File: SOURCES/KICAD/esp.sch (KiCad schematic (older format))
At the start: 14 parts, among them IC501 ESP32-WROOM-32U, Q501 Q_SS8050-G, Q502 Q_SS8050-G, SW501 SW_Push, X501 Conn_01x04, X502 Conn_01x05, X503 Conn_01x03, X504 HDR_01x06

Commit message: Updated BOM
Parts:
- C501, C503: Manufacturer (none) -> KEMET; pn (none) -> C0805C104K5RACTU
- C502: Manufacturer (none) -> Murata Electronics North America; pn (none) -> GRM21BR61E106MA73L
- IC501: Manufacturer (none) -> Espressif Systems; pn (none) -> ESP32-WROOM-32U
- Q501, Q502: Manufacturer (none) -> Comchip Technology; pn (none) -> SS8050-G
- R501, R502, R503: Manufacturer (none) -> Yageo; pn (none) -> RC0805FR-0710KL
- SW501: Manufacturer (none) -> Omron Electronics Inc-EMC Div; pn (none) -> B3U-1000P
- X501: Manufacturer (none) -> Molex, LLC; pn (none) -> 0022232041
- X502: Manufacturer (none) -> Molex, LLC; pn (none) -> 0530470510
- X503: Manufacturer (none) -> Molex, LLC; pn (none) -> 0530470310
- X504: Manufacturer (none) -> Sullins Connector Solutions; pn (none) -> PRPC006SAAN-RC
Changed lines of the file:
@@
 F 5 "Module" H 0   0   50  0001 C CNN "Value2"
 F 6 "1904-1026-1-ND" H 0   0   50  0001 C CNN "digikey"
+F 7 "Espressif Systems" H 0   0   50  0001 C CNN "Manufacturer"
+F 8 "ESP32-WROOM-32U" H 0   0   50  0001 C CNN "pn"
 	1    5600 3050
 	1    0    0    -1
@@
 F 5 "1% 0.125W Thick" H 3550 2525 39  0001 C CNN "Value2"
 F 6 "311-10.0KCRCT-ND" H 3550 2350 39  0001 C CNN "digikey"
+F 7 "Yageo" H 0   0   50  0001 C CNN "Manufacturer"
+F 8 "RC0805FR-0710KL" H 0   0   50  0001 C CNN "pn"
 	1    3550 2650
 	1    0    0    -1
@@
 F 5 "5% 50V X7R" H 3950 2600 39  0001 C CNN "Value2"
 F 6 "399-1170-1-ND" H 3950 2550 39  0001 C CNN "digikey"
+F 7 "KEMET" H 0   0   50  0001 C CNN "Manufacturer"
+F 8 "C0805C104K5RACTU" H 0   0   50  0001 C CNN "pn"
 	1    3950 2850
 	0    -1   -1   0
@@
 F 5 "5% 50V X7R" H 4350 2600 39  0001 C CNN "Value2"
 F 6 "399-1170-1-ND" H 4350 2550 39  0001 C CNN "digikey"
+F 7 "KEMET" H 0   0   50  0001 C CNN "Manufacturer"
+F 8 "C0805C104K5RACTU" H 0   0   50  0001 C CNN "pn"
 	1    4350 2850
 	0    -1   -1   0
@@
 F 5 "20% 25V X5R" H 4150 2600 39  0001 C CNN "Value2"
 F 6 "490-10748-1-ND" H 4150 2550 39  0001 C CNN "digikey"
+F 7 "Murata Electronics North America" H 0   0   50  0001 C CNN "Manufacturer"
+F 8 "GRM21BR61E106MA73L" H 0   0   50  0001 C CNN "pn"
 	1    4150 2850
 	0    -1   -1   0
@@
 F 5 "-" H 0   0   50  0001 C CNN "Value2"
 F 6 "???" H 0   0   50  0001 C CNN "digikey"
+F 7 "Molex, LLC" H 0   0   50  0001 C CNN "Manufacturer"
+F 8 "0022232041" H 0   0   50  0001 C CNN "pn"
 	1    8100 2100
 	1    0    0    1
@@
 F 5 "-" H 0   0   50  0001 C CNN "Value2"
 F 6 "???" H 0   0   50  0001 C CNN "digikey"
+F 7 "Molex, LLC" H 0   0   50  0001 C CNN "Manufacturer"
+F 8 "0530470510" H 0   0   50  0001 C CNN "pn"
 	1    8100 2950
 	1    0    0    1
@@
 F 5 "-" H 0   0   50  0001 C CNN "Value2"
 F 6 "???" H 0   0   50  0001 C CNN "digikey"
+F 7 "Molex, LLC" H 0   0   50  0001 C CNN "Manufacturer"
+F 8 "0530470310" H 0   0   50  0001 C CNN "pn"
 	1    8100 4000
 	1    0    0    1
@@
 F 5 "-" H 0   0   50  0001 C CNN "Value2"
 F 6 "???" H 0   0   50  0001 C CNN "digikey"
+F 7 "Sullins Connector Solutions" H 0   0   50  0001 C CNN "Manufacturer"
+F 8 "PRPC006SAAN-RC" H 0   0   50  0001 C CNN "pn"
 	1    7750 5200
 	1    0    0    -1
@@
 F 5 "1% 0.125W Thick" H 5250 5075 39  0001 C CNN "Value2"
 F 6 "311-10.0KCRCT-ND" H 5250 4900 39  0001 C CNN "digikey"
+F 7 "Yageo" H 0   0   50  0001 C CNN "Manufacturer"
+F 8 "RC0805FR-0710KL" H 0   0   50  0001 C CNN "pn"
 	1    5250 5200
 	1    0    0    -1
@@
 F 5 "1% 0.125W Thick" H 5250 5625 39  0001 C CNN "Value2"
 F 6 "311-10.0KCRCT-ND" H 5250 5450 39  0001 C CNN "digikey"
+F 7 "Yageo" H 0   0   50  0001 C CNN "Manufacturer"
+F 8 "RC0805FR-0710KL" H 0   0   50  0001 C CNN "pn"
 	1    5250 5750
 	1    0    0    -1
@@
 F 5 "-" H 5600 5200 50  0001 C CNN "Value2"
 F 6 "???" H 5600 5200 39  0001 C CNN "digikey"
+F 7 "Comchip Technology" H 0   0   50  0001 C CNN "Manufacturer"
+F 8 "SS8050-G" H 0   0   50  0001 C CNN "pn"
 	1    5600 5200
 	1    0    0    -1
@@
 F 5 "-" H 5600 5750 50  0001 C CNN "Value2"
 F 6 "???" H 5600 5750 39  0001 C CNN "digikey"
+F 7 "Comchip Technology" H 0   0   50  0001 C CNN "Manufacturer"
+F 8 "SS8050-G" H 0   0   50  0001 C CNN "pn"
 	1    5600 5750
 	1    0    0    1
@@
 F 5 "SWITCH TACTILE SPST-NO 0.05A 12V" H 3750 2850 39  0001 C CNN "Value2"
 F 6 "SW1020CT-ND" H 3750 2850 50  0001 C CNN "digikey"
+F 7 "Omron Electronics Inc-EMC Div" H 0   0   50  0001 C CNN "Manufacturer"
+F 8 "B3U-1000P" H 0   0   50  0001 C CNN "pn"
 	1    3750 2850
 	0    -1   -1   0

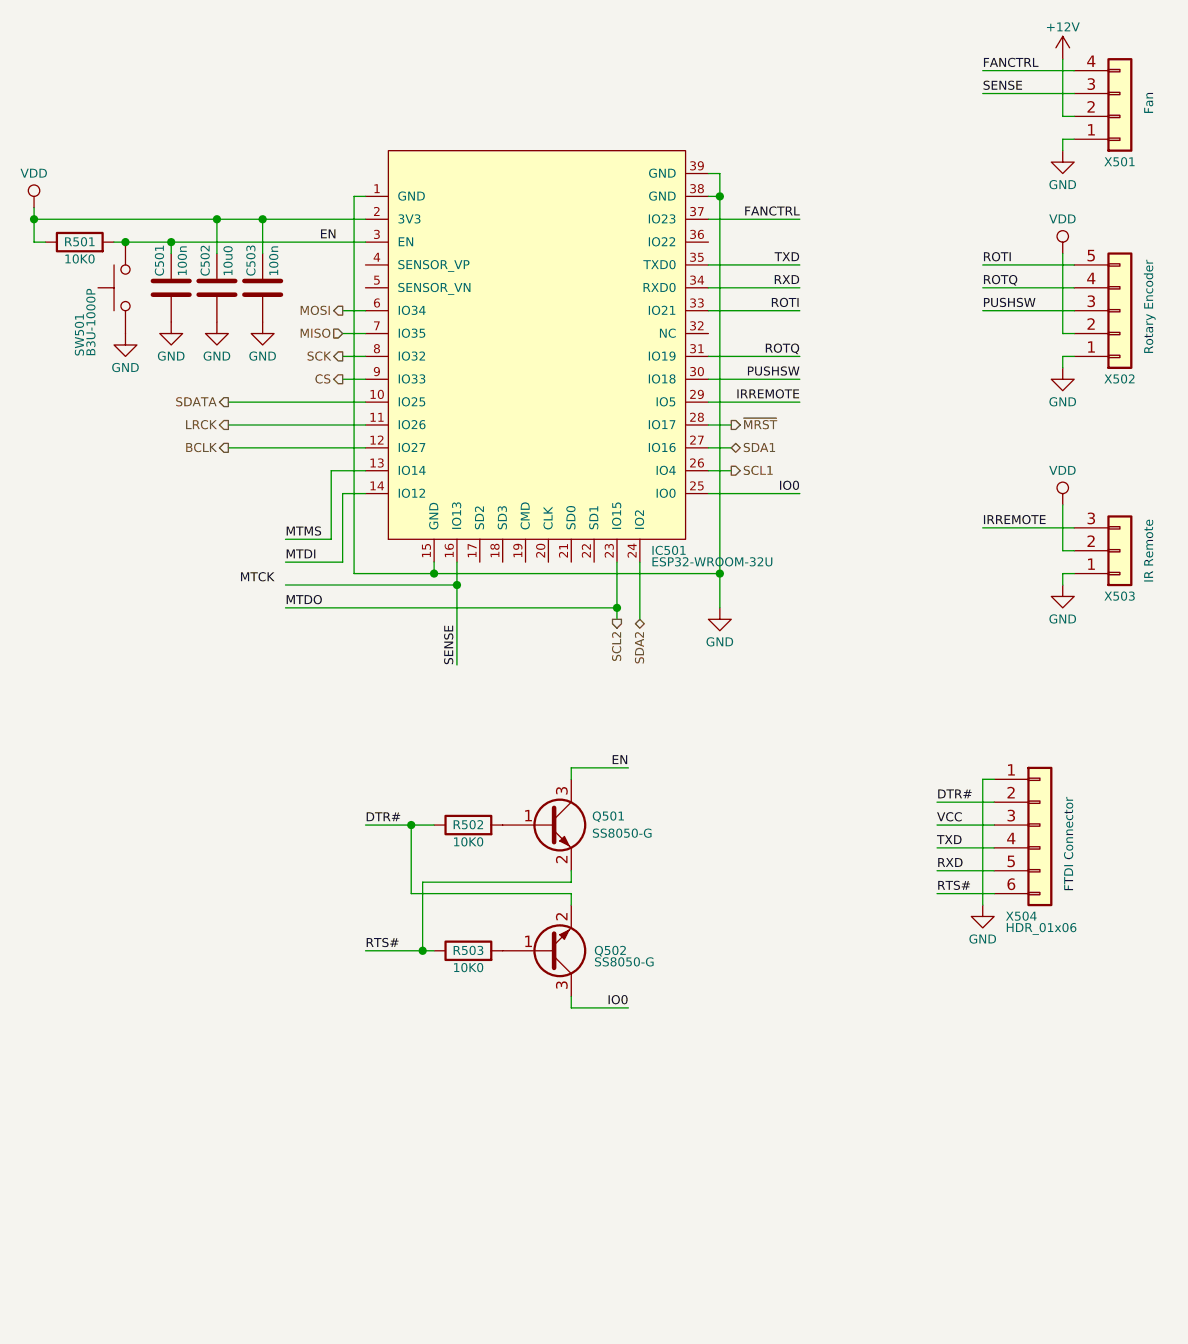
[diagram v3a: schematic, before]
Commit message: Added extra LDO for ESP32
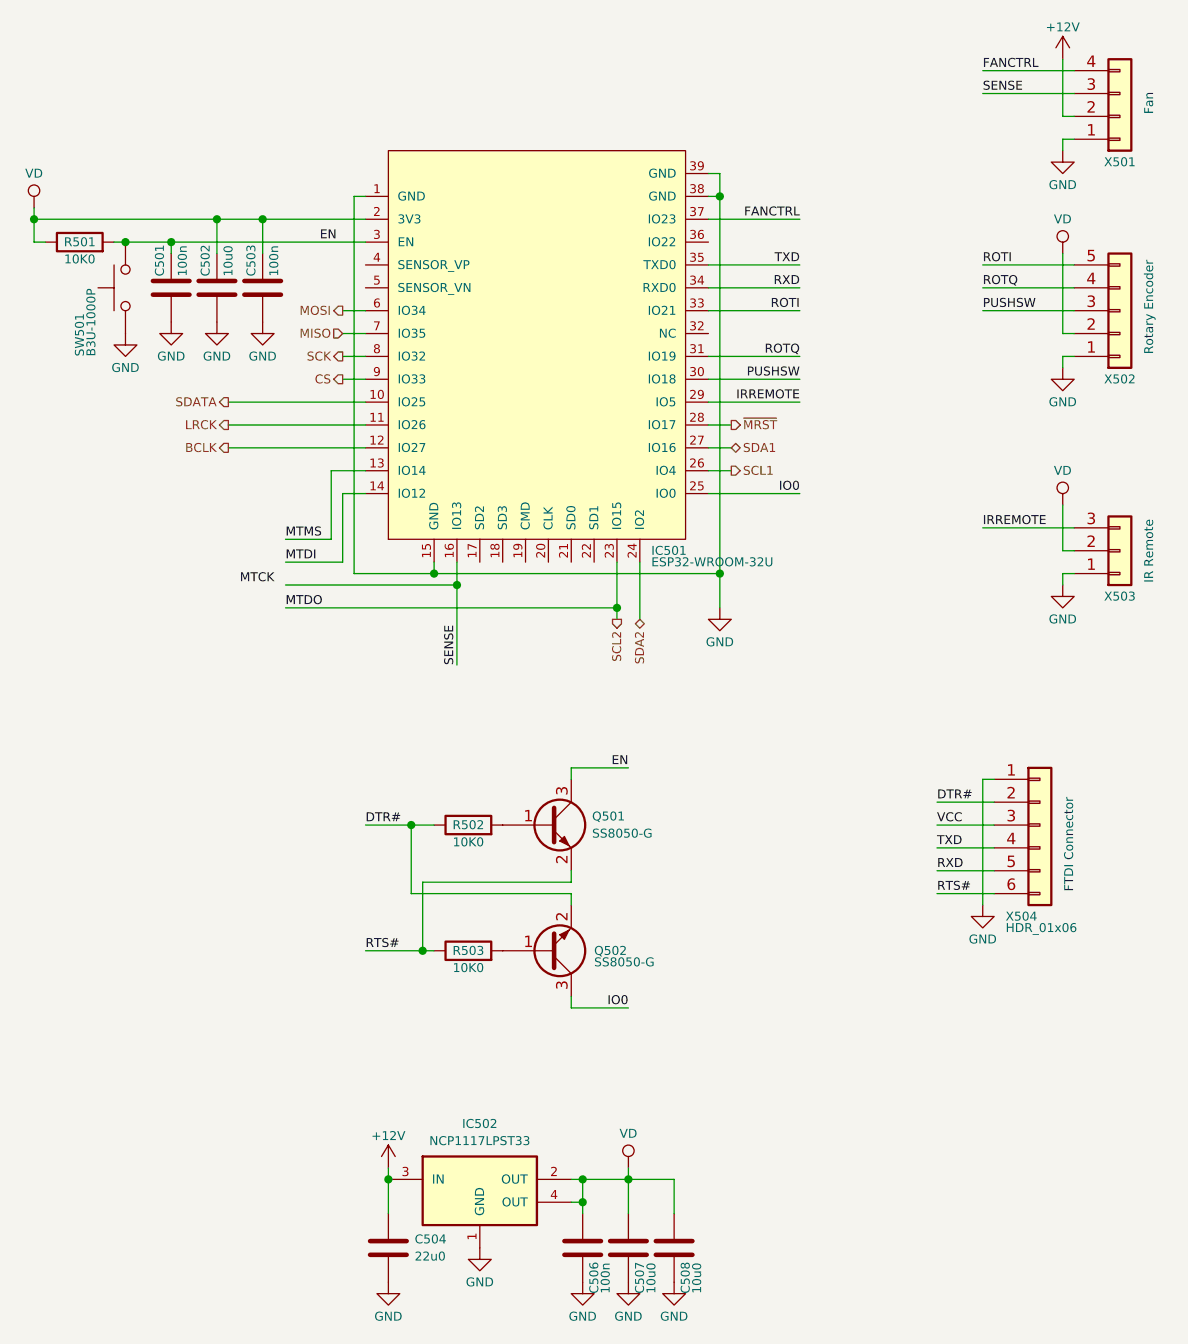
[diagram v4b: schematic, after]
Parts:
- added C504: CAP_22u0_10V_X5R_0805, rklib:C0805-X7R, symbol rk:CAP_22u0_10V_X5R_0805
- added C506: CAP_100n_50V_X7R_0805, rklib:C0805-X7R, symbol rk:CAP_100n_50V_X7R_0805
- added C507, C508: CAP_10u0_25V_X5R_0805, rklib:C0805-X7R, symbol rk:CAP_10u0_25V_X5R_0805
- added IC502: IC_NCP1117LPST33, rklib:SOT223, symbol rk:IC_NCP1117LPST33
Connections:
- net +12V: now also C504.1, IC502.3 (IN)
- net GND: now also C504.2, C506.2, C507.2, C508.2, IC502.1 (GND)
- net VDD renamed VD
- net VD: now also C506.1, C507.1, C508.1, IC502.2 (OUT), IC502.4 (OUT)

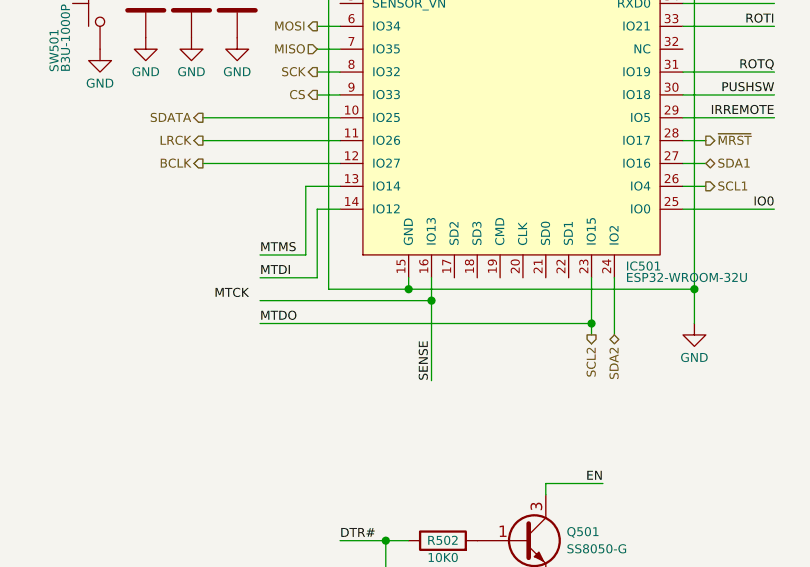
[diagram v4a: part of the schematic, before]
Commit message: Optimized ground plane
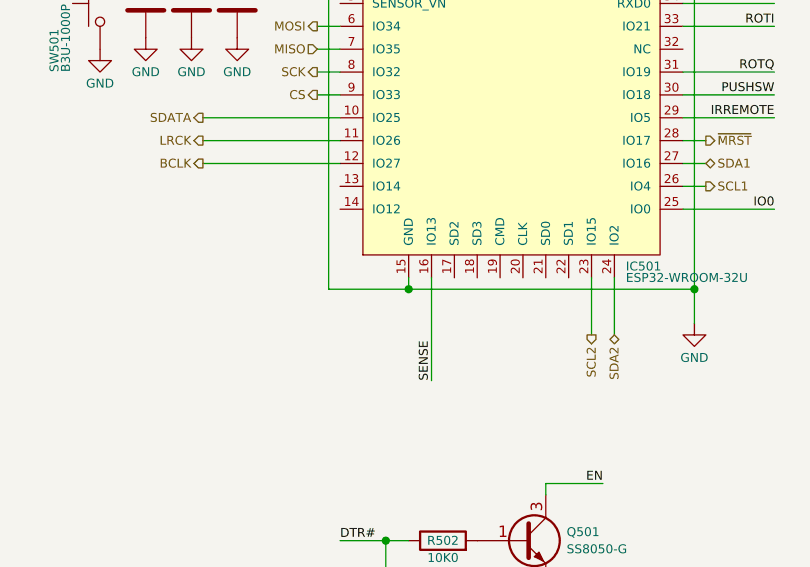
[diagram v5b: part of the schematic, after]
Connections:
- net MTDI: no longer names the net of IC501.14 (IO12)
- net MTMS: no longer names the net of IC501.13 (IO14)
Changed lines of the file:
@@
 	1    0    0    -1
 $EndComp
-Wire Wire Line
-	5200 4050 5200 4150
-Wire Wire Line
-	5200 4150 4450 4150
-Wire Wire Line
-	5900 4050 5900 4250
-Wire Wire Line
-	5900 4250 4450 4250
-Wire Wire Line
-	4800 3750 4700 3750
-Wire Wire Line
-	4700 3750 4700 4050
-Wire Wire Line
-	4700 4050 4450 4050
-Wire Wire Line
-	4800 3650 4650 3650
-Wire Wire Line
-	4650 3650 4650 3950
-Wire Wire Line
-	4650 3950 4450 3950
-Text Label 4450 3950 0    39   ~ 0
-MTMS
-Text Label 4450 4050 0    39   ~ 0
-MTDI
-Text Label 4250 4150 0    39   ~ 0
-MTCK
-Text Label 4450 4250 0    39   ~ 0
-MTDO
 Text HLabel 4700 2950 0    39   Output ~ 0
 MOSI
@@
 Text HLabel 6000 4300 3    39   BiDi ~ 0
 SDA2
-Connection ~ 5900 4250
 Wire Wire Line
 	6300 3450 6400 3450
-Connection ~ 5200 4150
 Wire Wire Line
 	6350 2450 6350 4100
@@
 Wire Wire Line
 	3350 2550 3350 2650
-Wire Wire Line
-	5900 4250 5900 4300
-Wire Wire Line
-	5200 4150 5200 4500
 $Comp
 L Connector_Generic:Conn_01x06 X504
@@
 	0    1    1    0
 $EndComp
+Wire Wire Line
+	5900 4050 5900 4300
+Wire Wire Line
+	5200 4050 5200 4500
 $EndSCHEMATC

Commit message: Updated BOM
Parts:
- Q501, Q502: digikey ??? -> 641-1790-1-ND
- X501: digikey ??? -> WM4202-ND
- X502: digikey ??? -> WM1734-ND
- X503: digikey ??? -> WM1732-ND
- X504: digikey ??? -> S1011EC-06-ND
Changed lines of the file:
@@
 F 4 "KK254-01x04" H 0   0   50  0001 C CNN "Value1"
 F 5 "-" H 0   0   50  0001 C CNN "Value2"
-F 6 "???" H 0   0   50  0001 C CNN "digikey"
+F 6 "WM4202-ND" H 0   0   50  0001 C CNN "digikey"
 F 7 "Molex, LLC" H 0   0   50  0001 C CNN "Manufacturer"
 F 8 "0022232041" H 0   0   50  0001 C CNN "pn"
@@
 F 4 "PB-01x05" H 0   0   50  0001 C CNN "Value1"
 F 5 "-" H 0   0   50  0001 C CNN "Value2"
-F 6 "???" H 0   0   50  0001 C CNN "digikey"
+F 6 "WM1734-ND" H 0   0   50  0001 C CNN "digikey"
 F 7 "Molex, LLC" H 0   0   50  0001 C CNN "Manufacturer"
 F 8 "0530470510" H 0   0   50  0001 C CNN "pn"
@@
 F 4 "PB-01x03" H 0   0   50  0001 C CNN "Value1"
 F 5 "-" H 0   0   50  0001 C CNN "Value2"
-F 6 "???" H 0   0   50  0001 C CNN "digikey"
+F 6 "WM1732-ND" H 0   0   50  0001 C CNN "digikey"
 F 7 "Molex, LLC" H 0   0   50  0001 C CNN "Manufacturer"
 F 8 "0530470310" H 0   0   50  0001 C CNN "pn"
@@
 F 4 "HDR-01x06" H 0   0   50  0001 C CNN "Value1"
 F 5 "-" H 0   0   50  0001 C CNN "Value2"
-F 6 "???" H 0   0   50  0001 C CNN "digikey"
+F 6 "S1011EC-06-ND" H 0   0   50  0001 C CNN "digikey"
 F 7 "Sullins Connector Solutions" H 0   0   50  0001 C CNN "Manufacturer"
 F 8 "PRPC006SAAN-RC" H 0   0   50  0001 C CNN "pn"
@@
 F 4 "SS8050-G" H 5791 5163 39  0000 L CNN "Value1"
 F 5 "-" H 5600 5200 50  0001 C CNN "Value2"
-F 6 "???" H 5600 5200 39  0001 C CNN "digikey"
+F 6 "641-1790-1-ND" H 5600 5200 39  0001 C CNN "digikey"
 F 7 "Comchip Technology" H 0   0   50  0001 C CNN "Manufacturer"
 F 8 "SS8050-G" H 0   0   50  0001 C CNN "pn"
@@
 F 4 "SS8050-G" H 5800 5800 39  0000 L CNN "Value1"
 F 5 "-" H 5600 5750 50  0001 C CNN "Value2"
-F 6 "???" H 5600 5750 39  0001 C CNN "digikey"
+F 6 "641-1790-1-ND" H 5600 5750 39  0001 C CNN "digikey"
 F 7 "Comchip Technology" H 0   0   50  0001 C CNN "Manufacturer"
 F 8 "SS8050-G" H 0   0   50  0001 C CNN "pn"
